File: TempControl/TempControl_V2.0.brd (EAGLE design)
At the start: 52.1 x 50.8 mm, 26 parts, among them J1 POWER_JACK, J3 10118194-0001LF_MICRO_USB, J4 SPARKFUN-CONNECTORS_6_PIN_SER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, J5 OLED_128_32, U1 328P, U2 L7805CV, Y1 16MHz

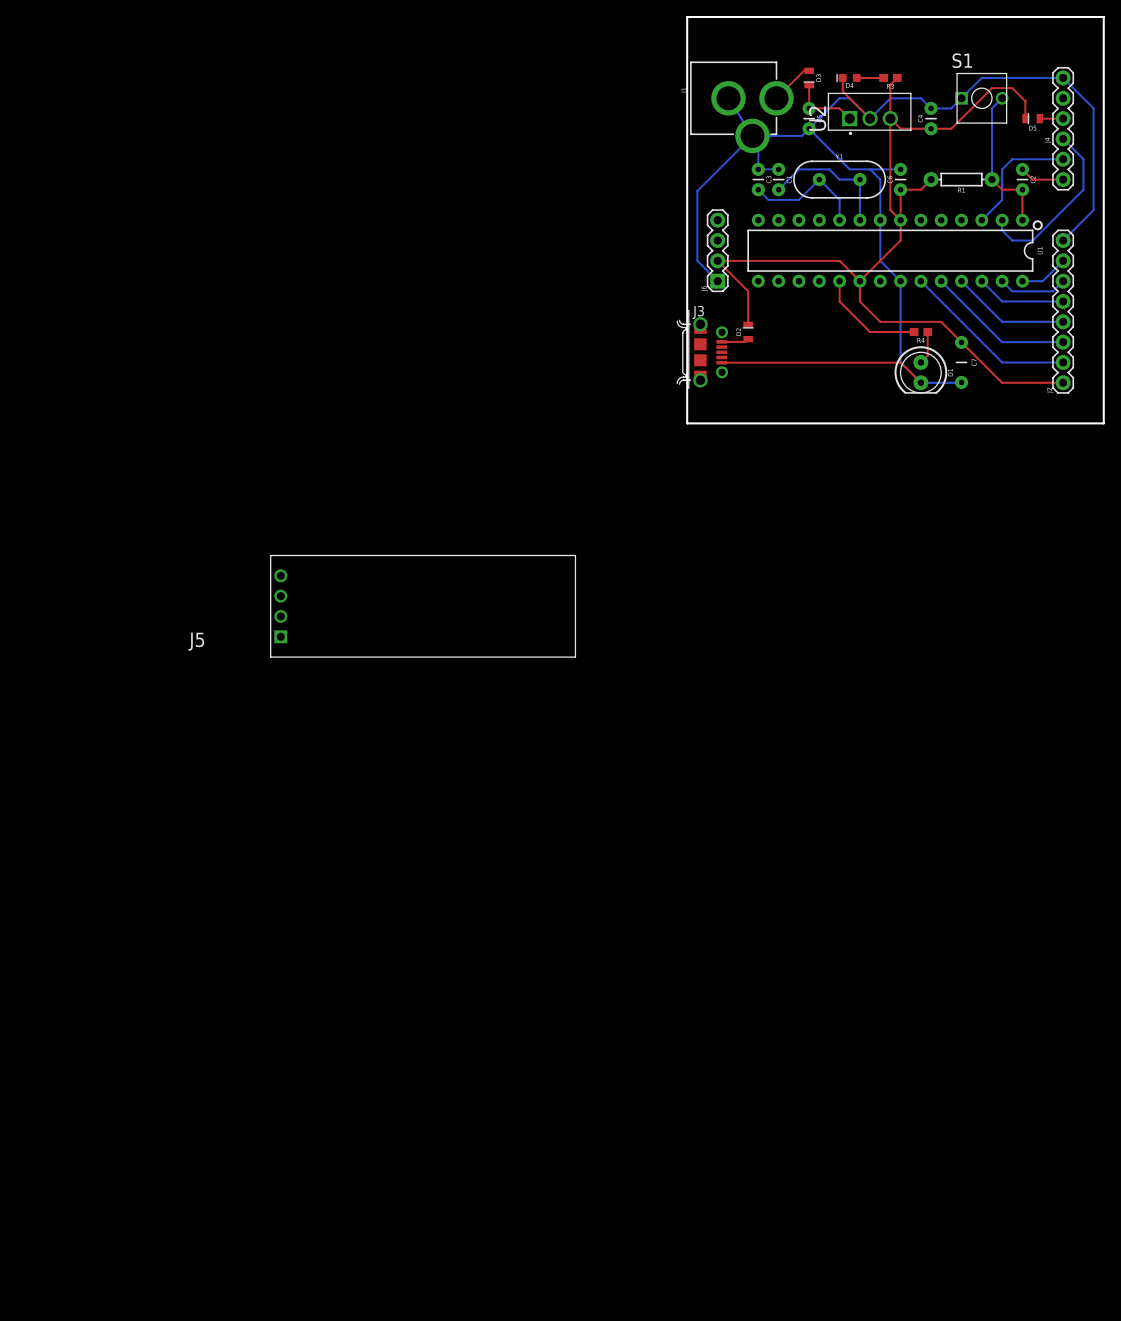
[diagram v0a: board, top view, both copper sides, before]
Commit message: - updated schematic and layout
- removed power jack
- added 3.3V regulator
- added OLED
- added level shifter
- added temp sensor
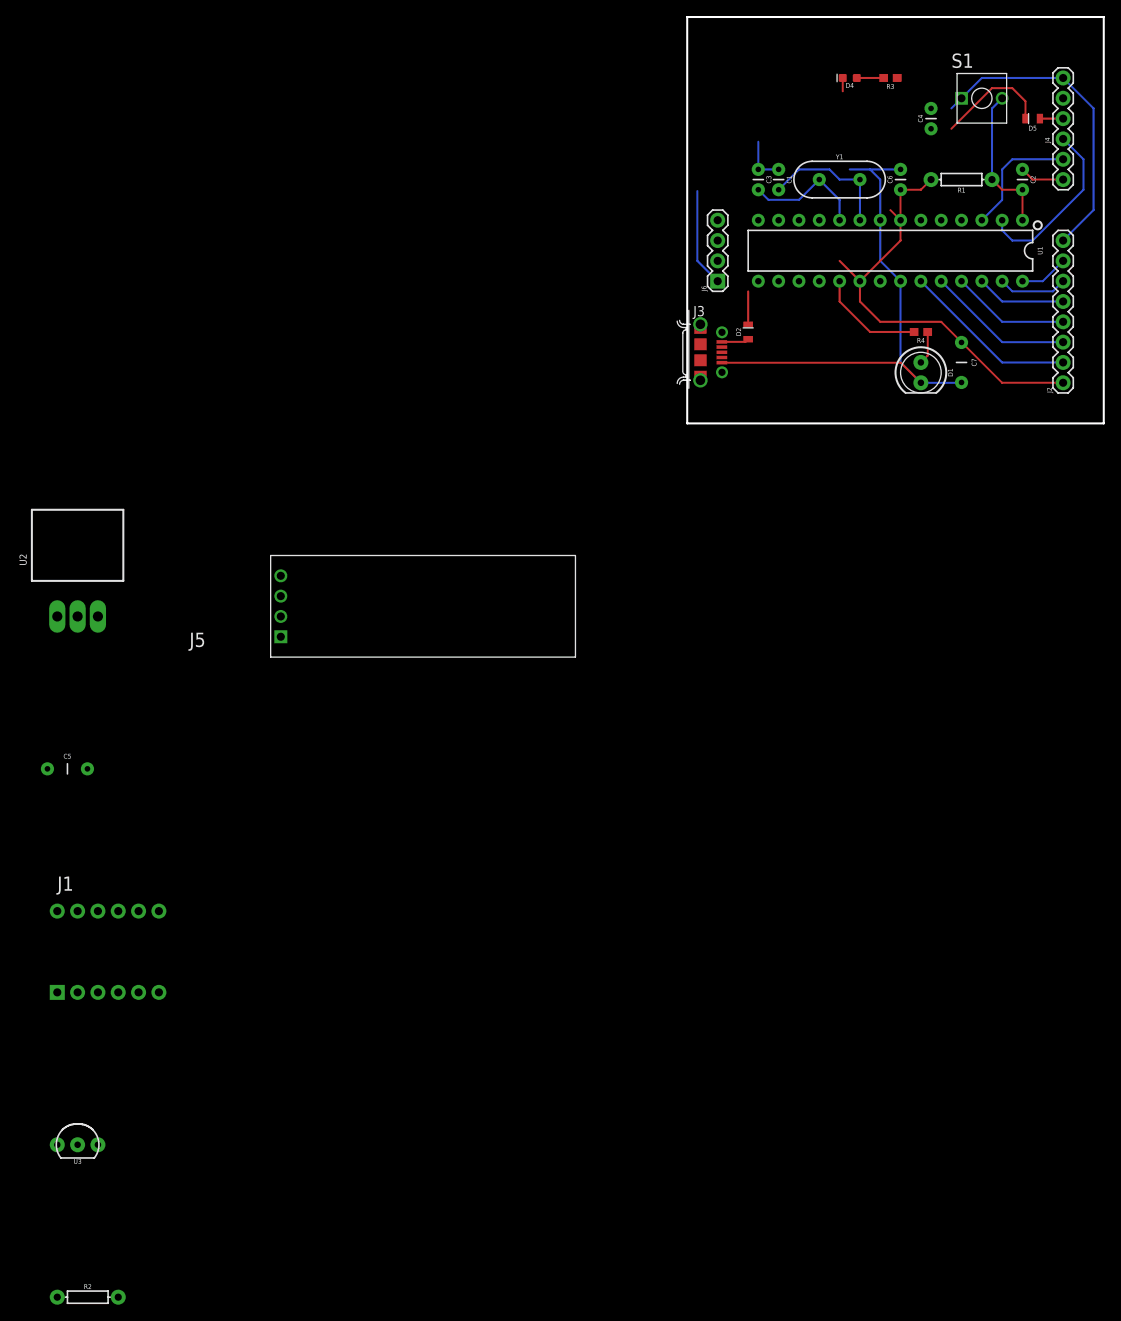
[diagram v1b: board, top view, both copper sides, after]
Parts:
- removed D3: SCHOTTKY_DIODE, TempControl:DIODE_0805
- added R2: 4.7KOHM, TempControl:AXIAL-0.3
- added U3: DS18B20, TempControl:TO-92-AMMO
- C5: value 0.33UF -> 10UF; device TempControl:CAP-PTH-2.54 -> TempControl:CAP-PTH-5MM
- J1: value POWER_JACK -> LEVEL_SHIFTER; device TempControl:POWER_JACK_PTH -> TempControl:LEVEL_SHIFTER
- U2: value L7805CV -> PMIC-LD1117V33(TO-220); device TempControl:TO254P460X1020X1945-3P -> TempControl:TO-220
- moved J1 135.3 mm to (-78.7, -22.9), turned to 0 degrees
- moved C5 123.3 mm to (-77.5, 5.08), turned to 0 degrees
- moved U2 111.3 mm to (-76.2, 35.6), turned to 0 degrees
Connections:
- removed net N$11: D3.1, J1.PWR
- removed net N$15: C5.1, D3.2, U2.1
- removed net N$5: J2.6, U1.27
- removed net N$6: J2.7, U1.28
- removed net SCL: J6.3
- removed net SDA: J6.4
- new net 3.3V: C5.1, J1.LV, J6.2, U2.3
- new net DQ: R2.P$1, U1.18, U3.2
- new net SCL_3.3V: J1.LV4, J6.3
- new net SCL_5V: J1.HV4, J2.7, U1.28
- new net SDA_3.3V: J1.LV3, J6.4
- new net SDA_5V: J1.HV3, J2.6, U1.27
- net GND: now also J1.HGND, J1.LGND, U3.1; no longer J1.GND, J1.GNDBREAK
- net VCC: now also J1.HV, R2.P$2, U2.1, U3.3; no longer J6.2, U2.3
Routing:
- net GND: track 183.5 -> 125.7 mm
- net VCC: track 119.5 -> 73.7 mm
- net SDA_5V: track 0.00 -> 8.67 mm
- net N$5: track 8.67 -> 0.00 mm
- net N$15: track 8.52 -> 0.00 mm
- net SCL_5V: track 0.00 -> 6.13 mm
- net N$6: track 6.13 -> 0.00 mm
- net N$11: track 5.50 -> 0.00 mm
